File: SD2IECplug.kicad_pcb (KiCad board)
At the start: 2 copper layers, 50 x 49.4 mm, 49 parts, among them J1 ISP, J2 X6, J3 Aux, J4 IEC, J5 C64-CassettePort, J6 C64-CassettePort, J7 Power, J8 X3, Q1 BSS138, Q2 BSS138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

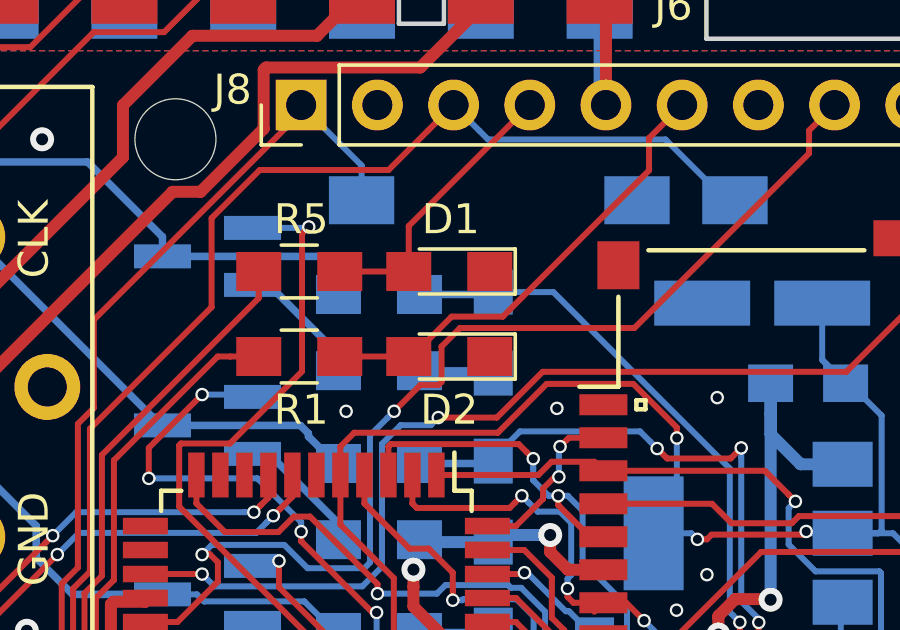
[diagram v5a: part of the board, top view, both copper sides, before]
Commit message: Corrected LED numbering.
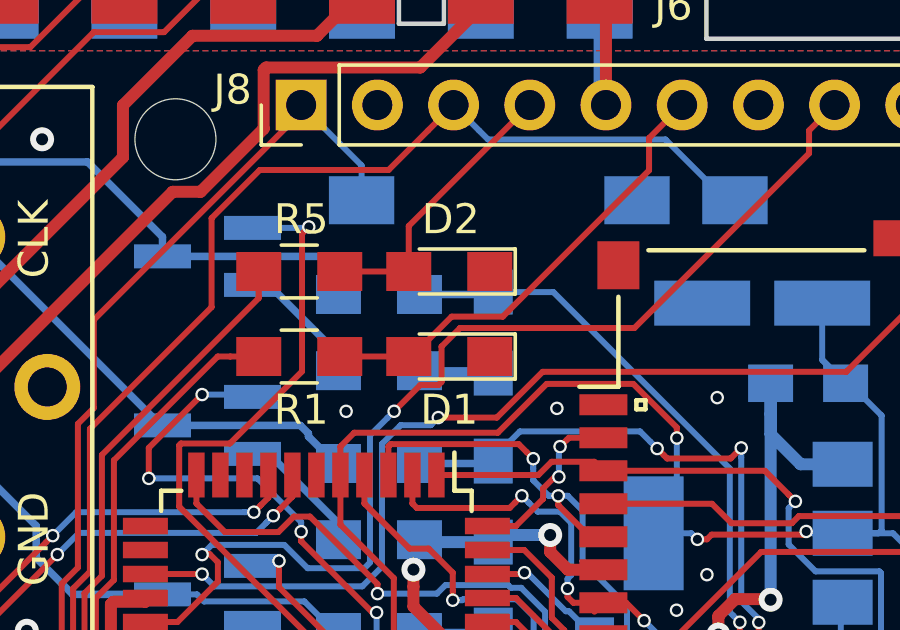
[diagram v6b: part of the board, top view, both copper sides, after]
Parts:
- U2: value LM1117-3.3 -> AMS1117-3.3
- renumbered D2 to D1, D1 to D2
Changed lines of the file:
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@@
       (effects (font (size 1 1) (thickness 0.15)) (justify mirror))
     )
-    (fp_text value LM1117-3.3 (at 0 -4.5 180) (layer B.Fab)
+    (fp_text value AMS1117-3.3 (at 0 -4.5 180) (layer B.Fab)
       (effects (font (size 1 1) (thickness 0.15)) (justify mirror))
     )
@@
     (tags "resistor 0805")
     (attr smd)
-    (fp_text reference D1 (at -0.05 4.574 180) (layer F.SilkS)
+    (fp_text reference D2 (at -0.05 4.574 180) (layer F.SilkS)
       (effects (font (size 1 1) (thickness 0.15)))
     )
@@
     (tags "resistor 0805")
     (attr smd)
-    (fp_text reference D2 (at 0 -4.61 180) (layer F.SilkS)
-      (effects (font (size 1 1) (thickness 0.15)))
-    )
+    (fp_text reference D1 (at 0 -4.61 180) (layer F.SilkS)
+      (effects (font (size 1 1) (thickness 0.15)))
+    )

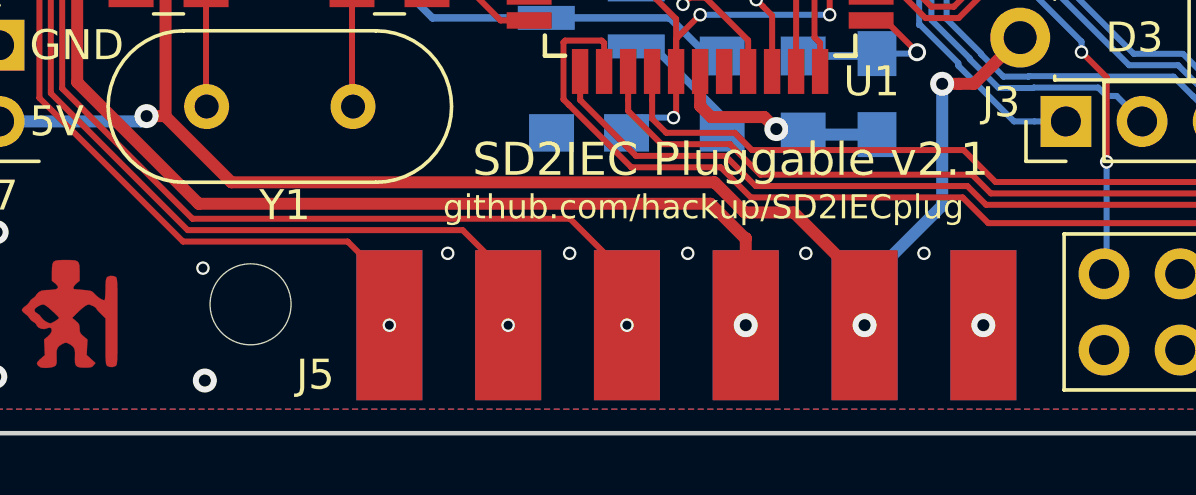
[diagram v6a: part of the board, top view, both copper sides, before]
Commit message: Moved connector pads to the edge.
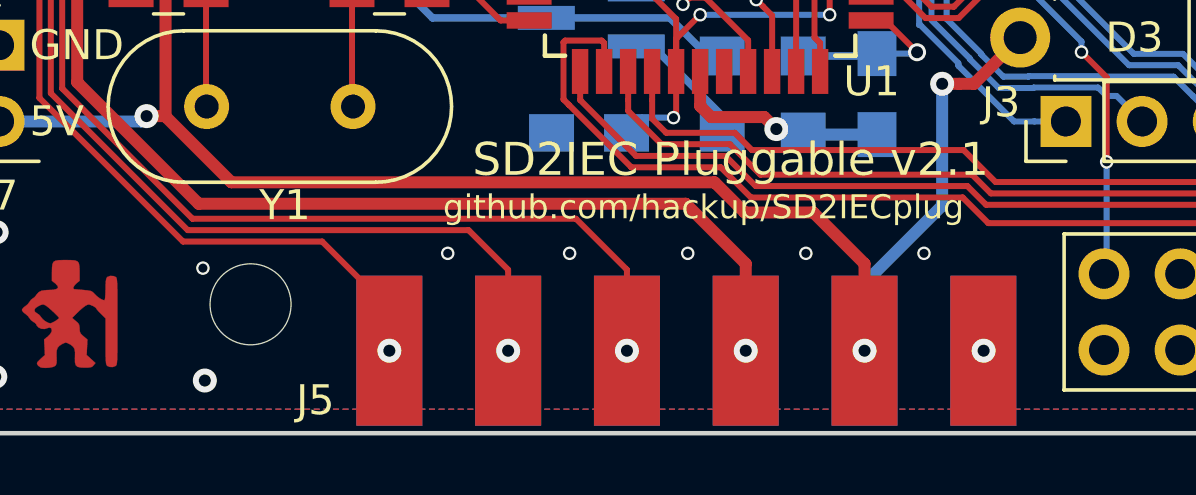
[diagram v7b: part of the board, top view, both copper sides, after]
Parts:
- moved J5 0.85 mm to (116.4, 91.1)
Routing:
- net Cas-Read: track 62.6 -> 65.2 mm
- net Cas-5V: track 93.9 -> 95.2 mm
- net Cas-Write: track 62.3 -> 63.5 mm
